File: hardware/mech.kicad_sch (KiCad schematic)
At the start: 6 parts

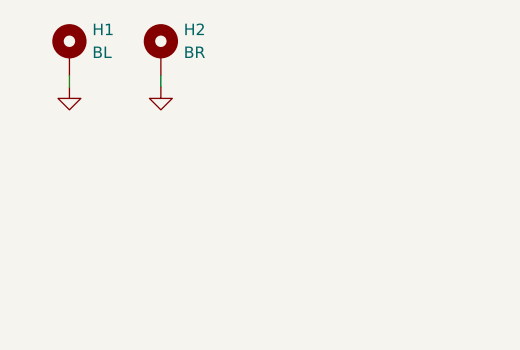
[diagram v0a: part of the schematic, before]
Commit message: layout 0 unconnected
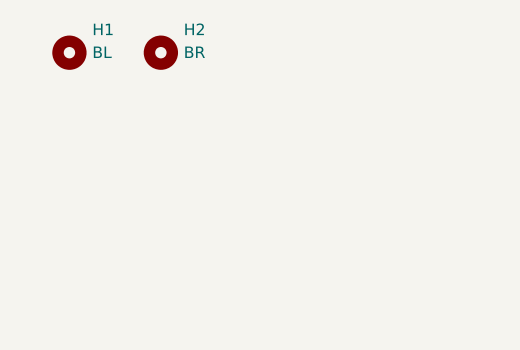
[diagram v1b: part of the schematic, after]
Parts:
- H1, H2: footprint MountingHole:MountingHole_2.5mm_Pad_Via -> MountingHole:MountingHole_2.2mm_M2_ISO7380; symbol Mechanical:MountingHole_Pad -> Mechanical:MountingHole
- N6: footprint Fiducial:Fiducial_0.5mm_Mask1.5mm -> Symbol:WEEE-Logo_4.2x6mm_SilkScreen
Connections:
- removed net GND: H1.1, H2.1
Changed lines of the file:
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@@
     (company "Frisius")
-  )
-  (wire (pts (xy 81.28 44.45) (xy 81.28 45.72))
-    (stroke (width 0) (type default) (color 0 0 0 0))
-  )
-  (wire (pts (xy 71.12 44.45) (xy 71.12 45.72))
-    (stroke (width 0) (type default) (color 0 0 0 0))
   )
   (symbol (lib_id "Mechanical:Housing") (at 128.27 82.55 0) (unit 1)
@@
       (effects (font (size 1.27 1.27)) (justify left))
     )
-    (property "Footprint" "Fiducial:Fiducial_0.5mm_Mask1.5mm" (id 2) (at 129.54 81.28 0)
+    (property "Footprint" "Symbol:WEEE-Logo_4.2x6mm_SilkScreen" (id 2) (at 129.54 81.28 0)
       (effects (font (size 1.27 1.27)) hide)
     )
@@
     )
   )
-  (symbol (lib_id "power:GND") (at 81.28 45.72 0) (unit 1)
-    (in_bom yes) (on_board yes) (fields_autoplaced)
-    (property "Reference" "#PWR070" (id 0) (at 81.28 52.07 0)
-      (effects (font (size 0.8 0.8)) hide)
-    )
-    (property "Value" "GND" (id 1) (at 81.28 50.8 0)
-      (effects (font (size 0.8 0.8)) hide)
-    )
-    (property "Footprint" "" (id 2) (at 81.28 45.72 0)
-      (effects (font (size 0.8 0.8)) hide)
-    )
-    (property "Datasheet" "" (id 3) (at 81.28 45.72 0)
-      (effects (font (size 0.8 0.8)) hide)
-    )
-    (pin "1")
-  )
-  (symbol (lib_id "power:GND") (at 71.12 45.72 0) (unit 1)
-    (in_bom yes) (on_board yes) (fields_autoplaced)
-    (property "Reference" "#PWR069" (id 0) (at 71.12 52.07 0)
-      (effects (font (size 0.8 0.8)) hide)
-    )
-    (property "Value" "GND" (id 1) (at 71.12 50.8 0)
-      (effects (font (size 0.8 0.8)) hide)
-    )
-    (property "Footprint" "" (id 2) (at 71.12 45.72 0)
-      (effects (font (size 0.8 0.8)) hide)
-    )
-    (property "Datasheet" "" (id 3) (at 71.12 45.72 0)
-      (effects (font (size 0.8 0.8)) hide)
-    )
-    (pin "1")
-  )
-  (symbol (lib_id "Mechanical:MountingHole_Pad") (at 81.28 41.91 0) (unit 1)
+  (symbol (lib_id "Mechanical:MountingHole") (at 81.28 41.91 0) (unit 1)
     (in_bom yes) (on_board yes) (fields_autoplaced)
     (property "Reference" "H2" (id 0) (at 83.82 39.3699 0)
@@
       (effects (font (size 1.27 1.27)) (justify left))
     )
-    (property "Footprint" "MountingHole:MountingHole_2.5mm_Pad_Via" (id 2) (at 81.28 41.91 0)
+    (property "Footprint" "MountingHole:MountingHole_2.2mm_M2_ISO7380" (id 2) (at 81.28 41.91 0)
       (effects (font (size 1.27 1.27)) hide)
     )
@@
       (effects (font (size 1.27 1.27)) hide)
     )
-    (pin "1")
   )
-  (symbol (lib_id "Mechanical:MountingHole_Pad") (at 71.12 41.91 0) (unit 1)
+  (symbol (lib_id "Mechanical:MountingHole") (at 71.12 41.91 0) (unit 1)
     (in_bom yes) (on_board yes) (fields_autoplaced)
     (property "Reference" "H1" (id 0) (at 73.66 39.3699 0)
@@
       (effects (font (size 1.27 1.27)) (justify left))
     )
-    (property "Footprint" "MountingHole:MountingHole_2.5mm_Pad_Via" (id 2) (at 71.12 41.91 0)
+    (property "Footprint" "MountingHole:MountingHole_2.2mm_M2_ISO7380" (id 2) (at 71.12 41.91 0)
       (effects (font (size 1.27 1.27)) hide)
     )
@@
       (effects (font (size 1.27 1.27)) hide)
     )
-    (pin "1")
   )
 )

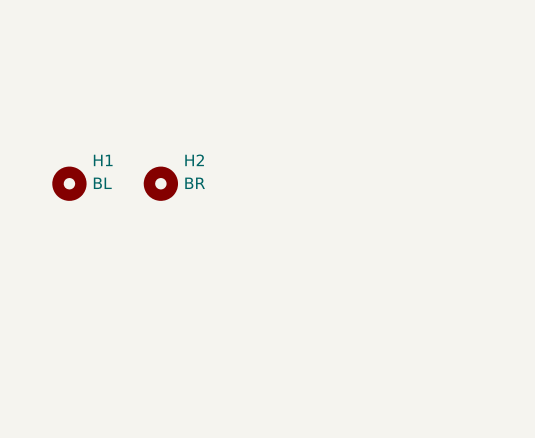
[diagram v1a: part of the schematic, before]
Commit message: merged in lcdboard test work
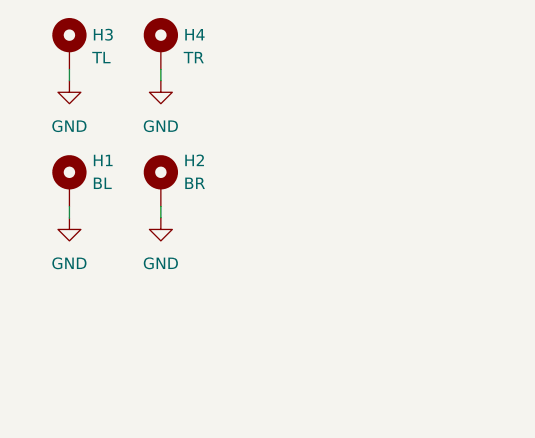
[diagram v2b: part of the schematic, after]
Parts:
- added H3: TL, Mounting_Wuerth:Mounting_Wuerth_WA-SMSI-M1.6_H2mm_9774020633, symbol Mechanical:MountingHole_Pad
- added H4: TR, Mounting_Wuerth:Mounting_Wuerth_WA-SMSI-M1.6_H2mm_9774020633, symbol Mechanical:MountingHole_Pad
- H1, H2: footprint MountingHole:MountingHole_2.2mm_M2_ISO7380 -> Mounting_Wuerth:Mounting_Wuerth_WA-SMSI-M1.6_H2mm_9774020633; symbol Mechanical:MountingHole -> Mechanical:MountingHole_Pad
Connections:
- new net GND: H1.1, H2.1, H3.1, H4.1
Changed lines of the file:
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@@
     (company "Frisius")
+  )
+  (wire (pts (xy 71.12 45.72) (xy 71.12 44.45))
+    (stroke (width 0) (type default) (color 0 0 0 0))
+  )
+  (wire (pts (xy 81.28 45.72) (xy 81.28 44.45))
+    (stroke (width 0) (type default) (color 0 0 0 0))
+  )
+  (wire (pts (xy 71.12 30.48) (xy 71.12 29.21))
+    (stroke (width 0) (type default) (color 0 0 0 0))
+  )
+  (wire (pts (xy 81.28 30.48) (xy 81.28 29.21))
+    (stroke (width 0) (type default) (color 0 0 0 0))
   )
   (symbol (lib_id "Mechanical:Housing") (at 128.27 82.55 0) (unit 1)
@@
     )
   )
+  (symbol (lib_id "power:GND") (at 81.28 45.72 0) (unit 1)
+    (in_bom yes) (on_board yes) (fields_autoplaced)
+    (property "Reference" "#PWR0151" (id 0) (at 81.28 52.07 0)
+      (effects (font (size 1.27 1.27)) hide)
+    )
+    (property "Value" "GND" (id 1) (at 81.28 50.8 0))
+    (property "Footprint" "" (id 2) (at 81.28 45.72 0)
+      (effects (font (size 1.27 1.27)) hide)
+    )
+    (property "Datasheet" "" (id 3) (at 81.28 45.72 0)
+      (effects (font (size 1.27 1.27)) hide)
+    )
+    (pin "1")
+  )
   (symbol (lib_id "Mechanical:Housing") (at 71.12 82.55 0) (unit 1)
     (in_bom yes) (on_board yes)
@@
       (effects (font (size 1.27 1.27)) hide)
     )
+  )
+  (symbol (lib_id "Mechanical:MountingHole_Pad") (at 71.12 26.67 0) (unit 1)
+    (in_bom yes) (on_board yes) (fields_autoplaced)
+    (property "Reference" "H3" (id 0) (at 73.66 25.3999 0)
+      (effects (font (size 1.27 1.27)) (justify left))
+    )
+    (property "Value" "TL" (id 1) (at 73.66 27.9399 0)
+      (effects (font (size 1.27 1.27)) (justify left))
+    )
+    (property "Footprint" "Mounting_Wuerth:Mounting_Wuerth_WA-SMSI-M1.6_H2mm_9774020633" (id 2) (at 71.12 26.67 0)
+      (effects (font (size 1.27 1.27)) hide)
+    )
+    (property "Datasheet" "~" (id 3) (at 71.12 26.67 0)
+      (effects (font (size 1.27 1.27)) hide)
+    )
+    (pin "1")
   )
   (symbol (lib_id "Mechanical:Housing") (at 154.94 82.55 0) (unit 1)
@@
     )
   )
-  (symbol (lib_id "Mechanical:MountingHole") (at 81.28 41.91 0) (unit 1)
+  (symbol (lib_id "Mechanical:MountingHole_Pad") (at 81.28 26.67 0) (unit 1)
+    (in_bom yes) (on_board yes) (fields_autoplaced)
+    (property "Reference" "H4" (id 0) (at 83.82 25.3999 0)
+      (effects (font (size 1.27 1.27)) (justify left))
+    )
+    (property "Value" "TR" (id 1) (at 83.82 27.9399 0)
+      (effects (font (size 1.27 1.27)) (justify left))
+    )
+    (property "Footprint" "Mounting_Wuerth:Mounting_Wuerth_WA-SMSI-M1.6_H2mm_9774020633" (id 2) (at 81.28 26.67 0)
+      (effects (font (size 1.27 1.27)) hide)
+    )
+    (property "Datasheet" "~" (id 3) (at 81.28 26.67 0)
+      (effects (font (size 1.27 1.27)) hide)
+    )
+    (pin "1")
+  )
+  (symbol (lib_id "power:GND") (at 71.12 45.72 0) (unit 1)
+    (in_bom yes) (on_board yes) (fields_autoplaced)
+    (property "Reference" "#PWR0152" (id 0) (at 71.12 52.07 0)
+      (effects (font (size 1.27 1.27)) hide)
+    )
+    (property "Value" "GND" (id 1) (at 71.12 50.8 0))
+    (property "Footprint" "" (id 2) (at 71.12 45.72 0)
+      (effects (font (size 1.27 1.27)) hide)
+    )
+    (property "Datasheet" "" (id 3) (at 71.12 45.72 0)
+      (effects (font (size 1.27 1.27)) hide)
+    )
+    (pin "1")
+  )
+  (symbol (lib_id "Mechanical:MountingHole_Pad") (at 81.28 41.91 0) (unit 1)
     (in_bom yes) (on_board yes) (fields_autoplaced)
     (property "Reference" "H2" (id 0) (at 83.82 39.3699 0)
@@
       (effects (font (size 1.27 1.27)) (justify left))
     )
-    (property "Footprint" "MountingHole:MountingHole_2.2mm_M2_ISO7380" (id 2) (at 81.28 41.91 0)
+    (property "Footprint" "Mounting_Wuerth:Mounting_Wuerth_WA-SMSI-M1.6_H2mm_9774020633" (id 2) (at 81.28 41.91 0)
       (effects (font (size 1.27 1.27)) hide)
     )
@@
       (effects (font (size 1.27 1.27)) hide)
     )
+    (pin "1")
   )
-  (symbol (lib_id "Mechanical:MountingHole") (at 71.12 41.91 0) (unit 1)
+  (symbol (lib_id "Mechanical:MountingHole_Pad") (at 71.12 41.91 0) (unit 1)
     (in_bom yes) (on_board yes) (fields_autoplaced)
     (property "Reference" "H1" (id 0) (at 73.66 39.3699 0)
@@
       (effects (font (size 1.27 1.27)) (justify left))
     )
-    (property "Footprint" "MountingHole:MountingHole_2.2mm_M2_ISO7380" (id 2) (at 71.12 41.91 0)
+    (property "Footprint" "Mounting_Wuerth:Mounting_Wuerth_WA-SMSI-M1.6_H2mm_9774020633" (id 2) (at 71.12 41.91 0)
       (effects (font (size 1.27 1.27)) hide)
     )
@@
       (effects (font (size 1.27 1.27)) hide)
     )
+    (pin "1")
+  )
+  (symbol (lib_id "power:GND") (at 81.28 30.48 0) (unit 1)
+    (in_bom yes) (on_board yes) (fields_autoplaced)
+    (property "Reference" "#PWR0149" (id 0) (at 81.28 36.83 0)
+      (effects (font (size 1.27 1.27)) hide)
+    )
+    (property "Value" "GND" (id 1) (at 81.28 35.56 0))
+    (property "Footprint" "" (id 2) (at 81.28 30.48 0)
+      (effects (font (size 1.27 1.27)) hide)
+    )
+    (property "Datasheet" "" (id 3) (at 81.28 30.48 0)
+      (effects (font (size 1.27 1.27)) hide)
+    )
+    (pin "1")
+  )
+  (symbol (lib_id "power:GND") (at 71.12 30.48 0) (unit 1)
+    (in_bom yes) (on_board yes) (fields_autoplaced)
+    (property "Reference" "#PWR0150" (id 0) (at 71.12 36.83 0)
+      (effects (font (size 1.27 1.27)) hide)
+    )
+    (property "Value" "GND" (id 1) (at 71.12 35.56 0))
+    (property "Footprint" "" (id 2) (at 71.12 30.48 0)
+      (effects (font (size 1.27 1.27)) hide)
+    )
+    (property "Datasheet" "" (id 3) (at 71.12 30.48 0)
+      (effects (font (size 1.27 1.27)) hide)
+    )
+    (pin "1")
   )
 )
